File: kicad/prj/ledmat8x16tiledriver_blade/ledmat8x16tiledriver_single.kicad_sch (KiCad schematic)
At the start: 17 parts, among them J1 Conn_01x10_Pin, J2 Conn_01x10_Pin, J3 Conn_02x08_Odd_Even, J4 Conn_02x08_Odd_Even, U1 TLC59283, U2 DMP31D7LDW, U3 DMP31D7LDW, U4 DMP31D7LDW, U5 DMP31D7LDW

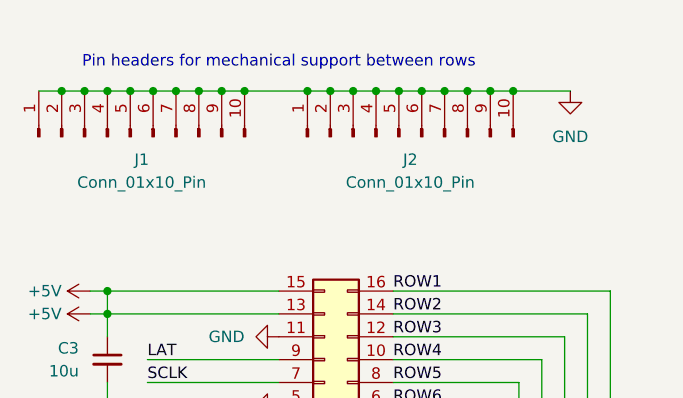
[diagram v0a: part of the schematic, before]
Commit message: Change headers for mounting to dnp on blade pcb
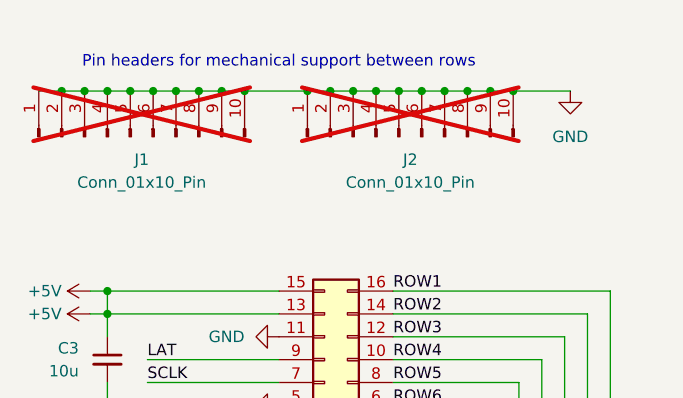
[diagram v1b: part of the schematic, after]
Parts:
- J1, J2: now not fitted
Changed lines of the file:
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@@
 		(in_bom yes)
 		(on_board yes)
-		(dnp no)
+		(dnp yes)
 		(fields_autoplaced yes)
 		(property "Reference" "J2"
@@
 		(in_bom yes)
 		(on_board yes)
-		(dnp no)
+		(dnp yes)
 		(fields_autoplaced yes)
 		(property "Reference" "J1"
